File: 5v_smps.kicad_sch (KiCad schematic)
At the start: 27 parts, among them U1 TPS62916RPYR

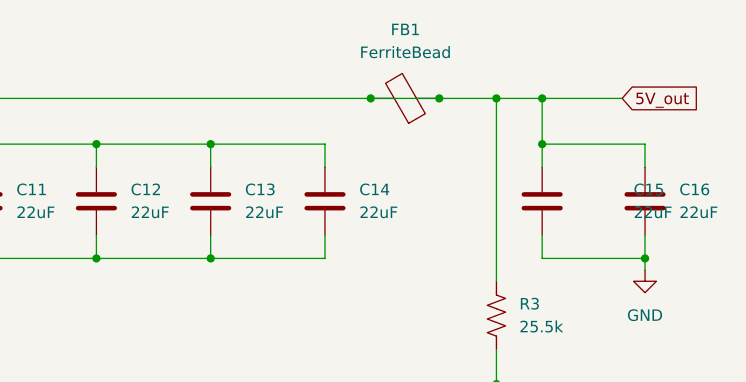
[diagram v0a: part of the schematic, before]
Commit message: Ferrite bead labeling on PCB fixed
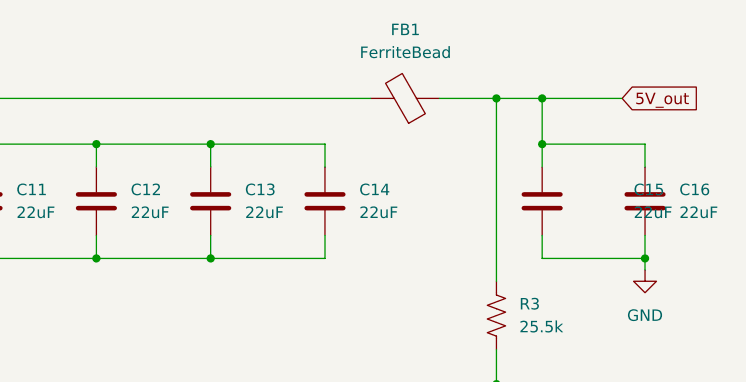
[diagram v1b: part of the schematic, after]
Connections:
- net 5V_out: no longer C10.1, C11.1, C12.1, C13.1, C14.1, C7.1, C8.1, C9.1, FB1.2, L1.1, R2.1, U1.4 (VO)
- new net VO: C10.1, C11.1, C12.1, C13.1, C14.1, C7.1, C8.1, C9.1, FB1.2, L1.1, R2.1, U1.4 (VO)
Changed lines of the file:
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@@
-	)
-	(junction
-		(at 335.28 59.69)
-		(diameter 0)
-		(color 0 0 0 0)
 	)
 	(junction
@@
 	)
 	(junction
-		(at 327.66 59.69)
-		(diameter 0)
-		(color 0 0 0 0)
-	)
-	(junction
 		(at 85.09 125.73)
 		(diameter 0)
@@
 		)
 		(stroke
-			(width 0)
-			(type default)
-		)
-	)
-	(wire
-		(pts
-			(xy 335.28 59.69) (xy 327.66 59.69)
-		)
-		(stroke
